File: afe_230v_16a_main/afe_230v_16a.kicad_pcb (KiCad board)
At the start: 2 copper layers, 146 x 86.4 mm, 77 parts, among them J1 MKDSN 2,5/ 6-5,08, J2 MKDS 1,5/ 6, J5 HBUS16, J6 pinheader_2x6_socket, U10 BlackPill_F4_SWI, U2 AD8538, U3 AD8538_dnp, U4 AQH3223A, U5 ACS711xLCTR-25AB, U6 AD8538_dnp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

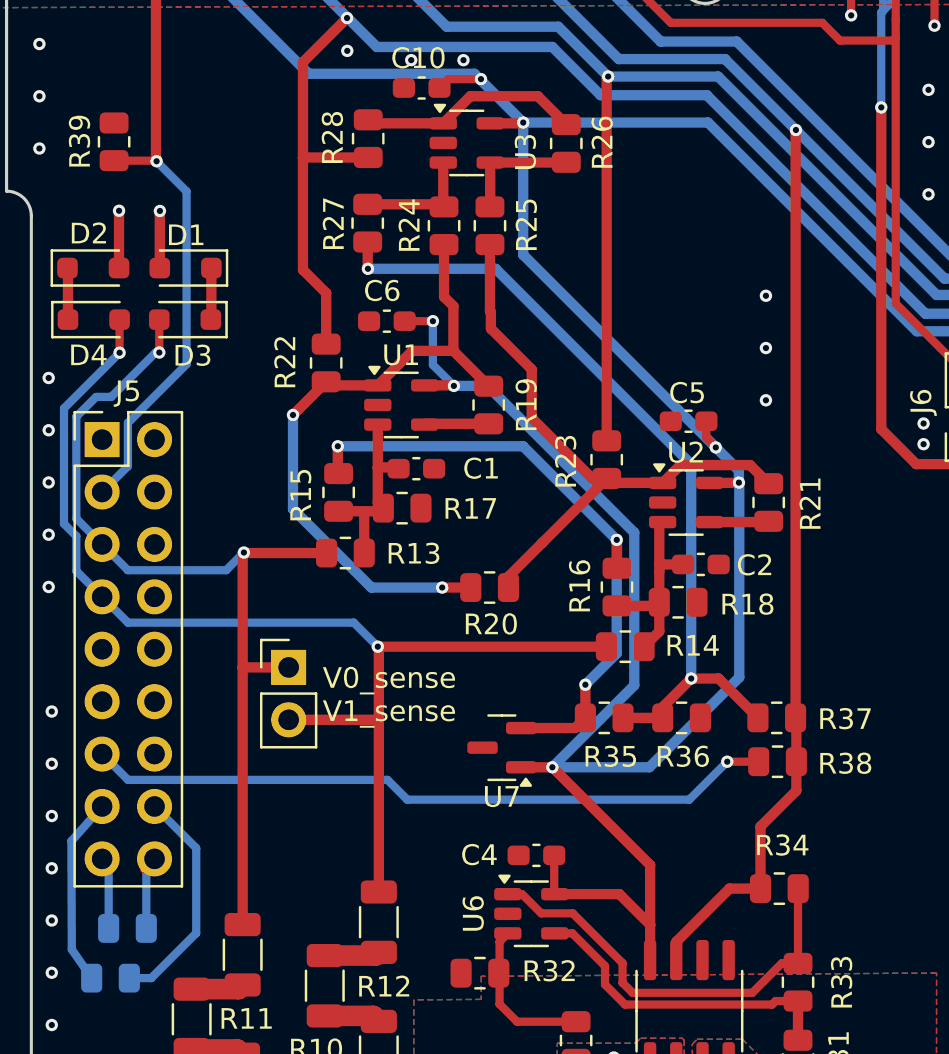
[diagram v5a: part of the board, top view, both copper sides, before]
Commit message: added and refined aug25 Mouser order
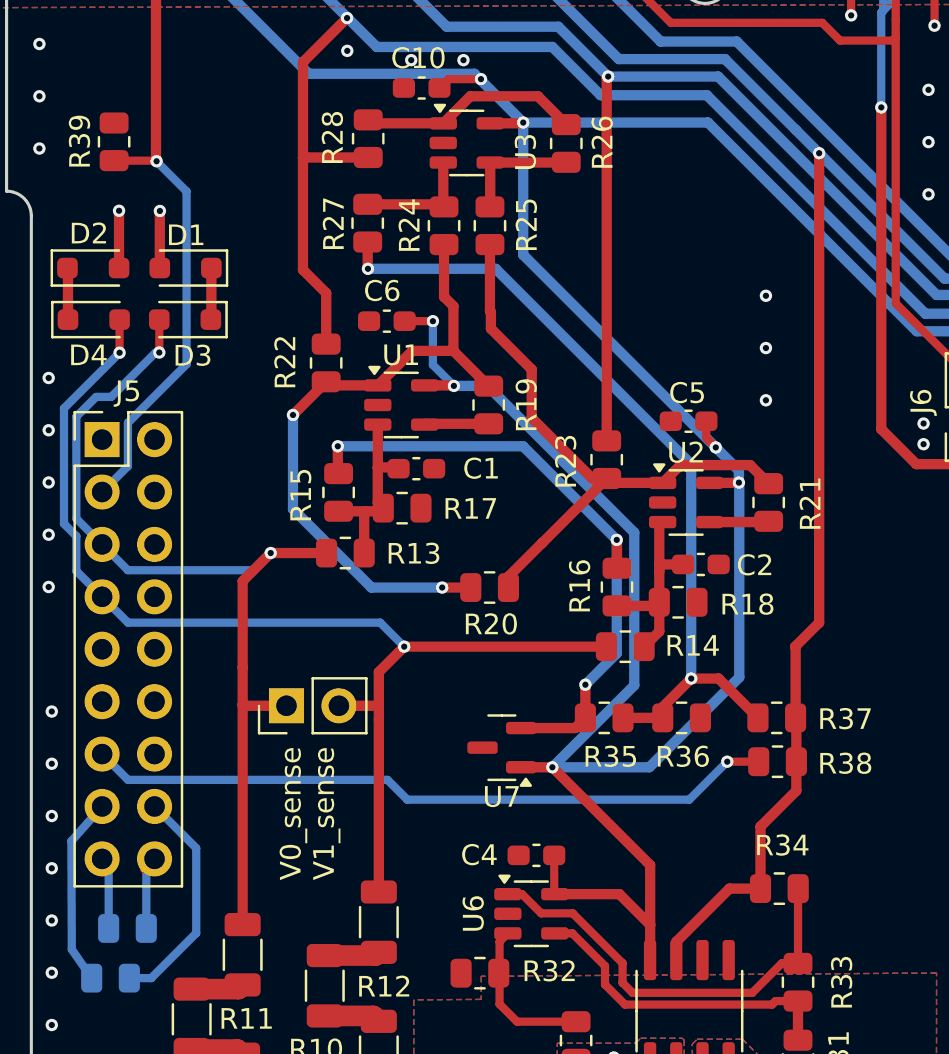
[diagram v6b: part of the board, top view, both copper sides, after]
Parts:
- moved REF** 1.86 mm to (131.5, 97.4), turned to 90 degrees
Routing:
- net /V1_sense: track 57.1 -> 55.2 mm
- net /A2: track 146.0 -> 145.3 mm
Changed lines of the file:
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@@
 	(footprint "Connector_PinHeader_2.54mm:PinHeader_1x02_P2.54mm_Vertical"
 		(layer "F.Cu")
-		(at 131.62 95.53)
+		(at 131.515 97.39 90)
 		(descr "Through hole straight pin header, 1x02, 2.54mm pitch, single row")
 		(tags "Through hole pin header THT 1x02 2.54mm single row")
 		(property "Reference" "REF**"
-			(at 0 -2.33 0)
+			(at 0 -2.33 90)
 			(layer "F.SilkS")
 			(hide yes)
@@
 		)
 		(property "Value" "PinHeader_1x02_P2.54mm_Vertical"
-			(at 0 4.87 0)
+			(at 0 4.87 90)
 			(layer "F.Fab")
 			(effects
@@
 		)
 		(property "Footprint" "Connector_PinHeader_2.54mm:PinHeader_1x02_P2.54mm_Vertical"
-			(at 0 0 0)
+			(at 0 0 90)
 			(unlocked yes)
 			(layer "F.Fab")
@@
 		)
 		(property "Datasheet" ""
-			(at 0 0 0)
+			(at 0 0 90)
 			(unlocked yes)
 			(layer "F.Fab")
@@
 		)
 		(property "Description" ""
-			(at 0 0 0)
+			(at 0 0 90)
 			(unlocked yes)
 			(layer "F.Fab")
@@
 		)
 		(fp_line
-			(start -1.33 1.27)
-			(end -1.33 3.87)
+			(start 1.33 1.27)
+			(end 1.33 3.87)
 			(stroke
 				(width 0.12)
@@
 		)
 		(fp_line
-			(start -1.33 3.87)
-			(end 1.33 3.87)
+			(start -1.33 1.27)
+			(end -1.33 3.87)
 			(stroke
 				(width 0.12)
@@
 		)
 		(fp_line
-			(start 1.33 1.27)
+			(start -1.33 3.87)
 			(end 1.33 3.87)
 			(stroke
@@
 		)
 		(fp_line
-			(start -1.8 -1.8)
-			(end -1.8 4.35)
+			(start 1.8 -1.8)
+			(end -1.8 -1.8)
 			(stroke
 				(width 0.05)
@@
 		)
 		(fp_line
-			(start -1.8 4.35)
-			(end 1.8 4.35)
+			(start -1.8 -1.8)
+			(end -1.8 4.35)
 			(stroke
 				(width 0.05)
@@
 		)
 		(fp_line
-			(start 1.8 -1.8)
-			(end -1.8 -1.8)
+			(start 1.8 4.35)
+			(end 1.8 -1.8)
 			(stroke
 				(width 0.05)
@@
 		)
 		(fp_line
-			(start 1.8 4.35)
-			(end 1.8 -1.8)
+			(start -1.8 4.35)
+			(end 1.8 4.35)
 			(stroke
 				(width 0.05)
@@
 		)
 		(fp_line
-			(start -1.27 -0.635)
-			(end -0.635 -1.27)
+			(start 1.27 -1.27)
+			(end 1.27 3.81)
 			(stroke
 				(width 0.1)
@@
 		)
 		(fp_line
-			(start -1.27 3.81)
-			(end -1.27 -0.635)
+			(start -0.635 -1.27)
+			(end 1.27 -1.27)
 			(stroke
 				(width 0.1)
@@
 		)
 		(fp_line
-			(start -0.635 -1.27)
-			(end 1.27 -1.27)
+			(start -1.27 -0.635)
+			(end -0.635 -1.27)
 			(stroke
 				(width 0.1)
@@
 		)
 		(fp_line
-			(start 1.27 -1.27)
-			(end 1.27 3.81)
+			(start 1.27 3.81)
+			(end -1.27 3.81)
 			(stroke
 				(width 0.1)
@@
 		)
 		(fp_line
-			(start 1.27 3.81)
-			(end -1.27 3.81)
+			(start -1.27 3.81)
+			(end -1.27 -0.635)
 			(stroke
 				(width 0.1)
@@
 		)
 		(fp_text user "${REFERENCE}"
-			(at 0 1.27 90)
+			(at 0 1.27 360)
 			(layer "F.Fab")
 			(effects
@@
 		)
 		(pad "1" thru_hole rect
-			(at 0 0)
+			(at 0 0 90)
 			(size 1.7 1.7)
 			(drill 1)
@@
 		)
 		(pad "2" thru_hole oval
-			(at 0 2.54)
+			(at 0 2.54 90)
 			(size 1.7 1.7)
 			(drill 1)
@@
 	)
 	(gr_text "V0_sense\nV1_sense"
-		(at 133.27 98.25 0)
+		(at 133.93 105.85 90)
 		(layer "F.SilkS")
 		(effects
@@
 	)
 	(segment
-		(start 129.475 89.9875)
-		(end 129.45 89.9625)
+		(start 129.43 97.39)
+		(end 129.39 97.35)
 		(width 0.5)
 		(layer "F.Cu")
@@
 	)
 	(segment
-		(start 129.39 95.53)
-		(end 129.39 90.0225)
+		(start 129.39 107.995)
+		(end 129.39 97.35)
 		(width 0.5)
 		(layer "F.Cu")
@@
 	)
 	(segment
-		(start 129.39 90.0225)
-		(end 129.45 89.9625)
+		(start 131.515 97.39)
+		(end 129.43 97.39)
 		(width 0.5)
 		(layer "F.Cu")
@@
 	)
 	(segment
-		(start 131.62 95.53)
+		(start 125.35 78.675)
+		(end 125.35 80.27)
+		(width 0.4)
+		(layer "F.Cu")
+		(net 6)
+	)
+	(segment
+		(start 129.39 97.35)
 		(end 129.39 95.53)
 		(width 0.5)
@@
 	)
 	(segment
-		(start 129.39 107.995)
-		(end 129.39 95.53)
+		(start 133.4575 89.9875)
+		(end 130.75 89.9875)
 		(width 0.5)
 		(layer "F.Cu")
@@
 	)
 	(segment
-		(start 125.35 78.675)
-		(end 125.35 80.27)
-		(width 0.4)
+		(start 129.39 91.3475)
+		(end 130.75 89.9875)
+		(width 0.5)
 		(layer "F.Cu")
 		(net 6)
 	)
 	(segment
-		(start 133.4575 89.9875)
-		(end 129.475 89.9875)
+		(start 129.39 95.53)
+		(end 129.39 91.3475)
 		(width 0.5)
 		(layer "F.Cu")
@@
 	)
 	(via
-		(at 129.45 89.9625)
+		(at 130.75 89.9875)
 		(size 0.6)
 		(drill 0.3)
@@
 	)
 	(segment
-		(start 123.83 90.82)
-		(end 122.58 89.57)
-		(width 0.4)
-		(layer "B.Cu")
-		(net 6)
-	)
-	(segment
 		(start 121.33 83.38)
 		(end 122.29 82.42)
@@
 	)
 	(segment
-		(start 128.5925 90.82)
+		(start 130.75 89.9875)
+		(end 129.9175 90.82)
+		(width 0.4)
+		(layer "B.Cu")
+		(net 6)
+	)
+	(segment
+		(start 129.9175 90.82)
 		(end 123.83 90.82)
 		(width 0.4)
@@
 	)
 	(segment
-		(start 125.17 80.27)
-		(end 125.35 80.27)
+		(start 123.83 90.82)
+		(end 122.58 89.57)
 		(width 0.4)
 		(layer "B.Cu")
@@
 	)
 	(segment
-		(start 129.45 89.9625)
-		(end 128.5925 90.82)
+		(start 125.17 80.27)
+		(end 125.35 80.27)
 		(width 0.4)
 		(layer "B.Cu")
@@
 	)
 	(segment
-		(start 135.99 94.575)
-		(end 135.94 94.525)
+		(start 135.95 97.39)
+		(end 135.99 97.35)
+		(width 0.5)
+		(layer "F.Cu")
+		(net 7)
+	)
+	(segment
+		(start 147.02 94.525)
+		(end 137.22 94.525)
 		(width 0.5)
 		(layer "F.Cu")
@@
 	)
 	(segment
-		(start 135.99 98.07)
-		(end 135.99 94.575)
+		(start 134.055 97.39)
+		(end 135.95 97.39)
 		(width 0.5)
 		(layer "F.Cu")
@@
 	)
 	(segment
-		(start 147.02 94.525)
-		(end 135.94 94.525)
+		(start 135.99 95.755)
+		(end 137.22 94.525)
+		(width 0.5)
+		(layer "F.Cu")
+		(net 7)
+	)
+	(segment
+		(start 135.99 98.07)
+		(end 135.99 97.35)
 		(width 0.5)
 		(layer "F.Cu")
@@
 	)
 	(segment
-		(start 123.425 78.675)
-		(end 123.425 80.28)
-		(width 0.4)
+		(start 135.99 97.35)
+		(end 135.99 95.755)
+		(width 0.5)
 		(layer "F.Cu")
 		(net 7)
 	)
 	(segment
-		(start 131.62 98.07)
-		(end 135.99 98.07)
-		(width 0.5)
+		(start 123.425 78.675)
+		(end 123.425 80.28)
+		(width 0.4)
 		(layer "F.Cu")
 		(net 7)
 	)
 	(via
-		(at 135.94 94.525)
+		(at 137.22 94.525)
 		(size 0.6)
 		(drill 0.3)
@@
 	)
 	(segment
-		(start 135.94 94.525)
-		(end 134.775 93.36)
+		(start 123.83 93.36)
+		(end 122.58 92.11)
 		(width 0.4)
 		(layer "B.Cu")
@@
 	)
 	(segment
-		(start 121.33 89.168528)
-		(end 120.73 88.568528)
+		(start 136.055 93.36)
+		(end 123.83 93.36)
 		(width 0.4)
 		(layer "B.Cu")
@@
 	)
 	(segment
-		(start 122.58 92.11)
-		(end 121.33 90.86)
+		(start 121.33 89.168528)
+		(end 120.73 88.568528)
 		(width 0.4)
 		(layer "B.Cu")
@@
 	)
 	(segment
-		(start 123.83 93.36)
-		(end 122.58 92.11)
+		(start 122.58 92.11)
+		(end 121.33 90.86)
 		(width 0.4)
 		(layer "B.Cu")
@@
 	)
 	(segment
-		(start 121.33 90.86)
-		(end 121.33 89.168528)
+		(start 137.22 94.525)
+		(end 136.055 93.36)
 		(width 0.4)
 		(layer "B.Cu")
@@
 	)
 	(segment
-		(start 134.775 93.36)
-		(end 123.83 93.36)
+		(start 121.33 90.86)
+		(end 121.33 89.168528)
 		(width 0.4)
 		(layer "B.Cu")
@@
 	)
 	(segment
+		(start 156.1875 94.5375)
+		(end 156.1875 97.975)
+		(width 0.5)
+		(layer "F.Cu")
+		(net 14)
+	)
+	(segment
 		(start 239.03 84.802944)
 		(end 240.512944 83.32)
@@
 	)
 	(segment
+		(start 157.33 70.61)
+		(end 157.33 93.36)
+		(width 0.5)
+		(layer "F.Cu")
+		(net 14)
+	)
+	(segment
 		(start 150.41 108.825001)
 		(end 152.985001 106.25)
@@
 	)
 	(segment
-		(start 156.205 69.485)
-		(end 156.1875 69.5025)
+		(start 157.33 93.36)
+		(end 156.17 94.52)
 		(width 0.5)
 		(layer "F.Cu")
@@
 	)
 	(segment
-		(start 156.1875 69.5025)
-		(end 156.1875 97.975)
-		(width 0.5)
-		(layer "F.Cu")
-		(net 14)
-	)
-	(segment
 		(start 171.83 78.52)
 		(end 174.96 81.65)
@@
 	)
 	(segment
+		(start 156.17 94.52)
+		(end 156.1875 94.5375)
+		(width 0.5)
+		(layer "F.Cu")
+		(net 14)
+	)
+	(segment
 		(start 150.41 109.8)
 		(end 150.41 108.825001)
@@
 	)
 	(via
-		(at 156.205 69.485)
+		(at 157.33 70.61)
 		(size 0.6)
 		(drill 0.3)
